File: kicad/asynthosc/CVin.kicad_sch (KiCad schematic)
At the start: 11 parts, among them J14 AudioJack3, SW4 SW_DIP_x02, U9 MCP6004

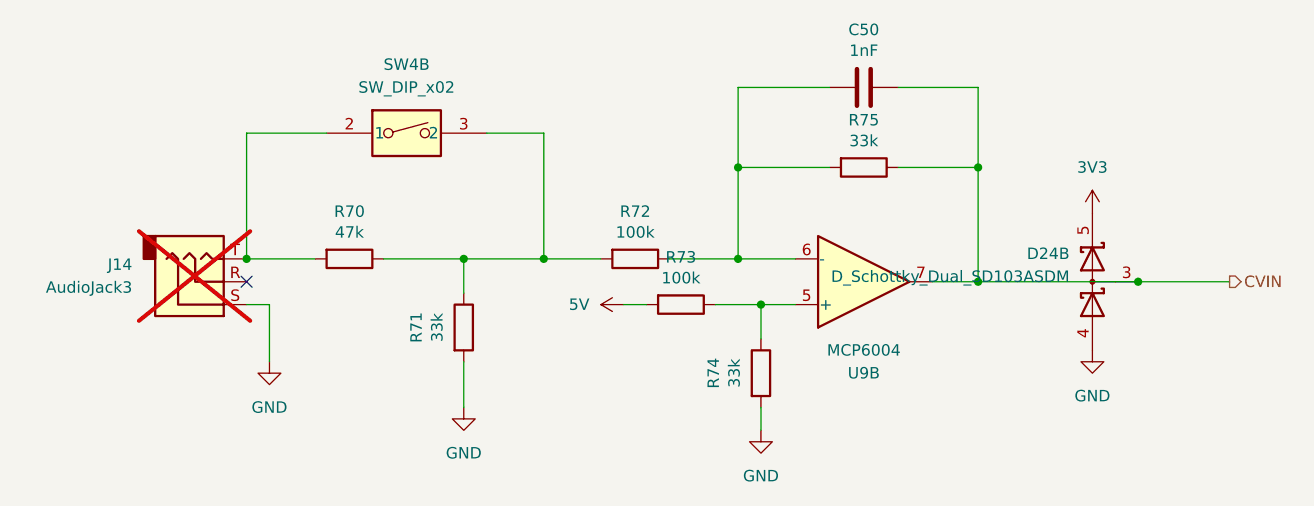
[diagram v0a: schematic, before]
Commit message: bom: fab: switch component due to fab shortage
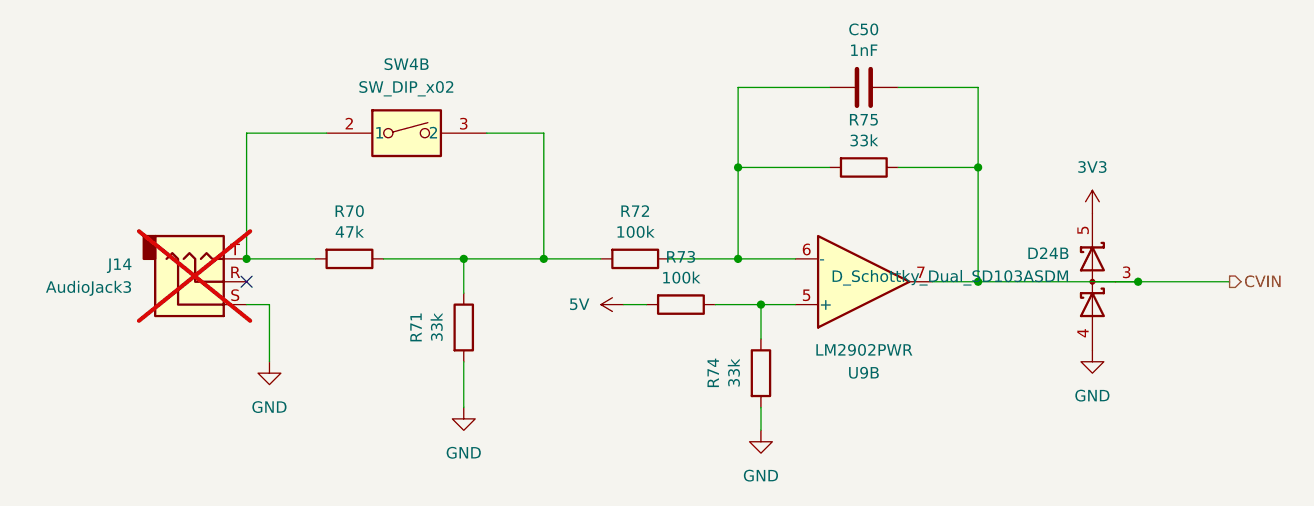
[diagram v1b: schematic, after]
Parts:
- U9: value MCP6004 -> LM2902PWR; LCSC C627416 -> C46864; Manufacturer Microchip -> TI; RefNum MCP6004T-E/ST -> LM2902PWR
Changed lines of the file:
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@@
 			)
 		)
-		(property "Value" "MCP6004"
+		(property "Value" "LM2902PWR"
 			(at 113.03 62.23 0)
 			(effects
@@
 			)
 		)
-		(property "LCSC" "C627416"
+		(property "LCSC" "C46864"
 			(at 113.03 54.61 0)
 			(effects
@@
 			)
 		)
-		(property "Manufacturer" "Microchip"
+		(property "Manufacturer" "TI"
 			(at 113.03 54.61 0)
 			(effects
@@
 			)
 		)
-		(property "RefNum" " MCP6004T-E/ST"
+		(property "RefNum" " LM2902PWR"
 			(at 113.03 54.61 0)
 			(effects

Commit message: sch: bump to kicad 9
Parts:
- renumbered C50 to C34, D24 to D22, J14 to J8, R70 to R27, R71 to R28, R72 to R29, R73 to R30, R74 to R31, R75 to R32, SW4 to SW3, U9 to U8
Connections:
- net 3V3: now also D22.2 (K); no longer D22.5 (K)
- net CVIN: now also D22.6 (common), U8.1; no longer D22.3 (common), U8.7
- net GND: now also D22.1 (A); no longer D22.4 (A)
- net at C34.2, R29.1, R32.2: now also U8.2 (-); no longer U8.6 (-)
- net at R27.1, R28.1, R29.2: now also SW3.4 (2); no longer SW3.3 (2)
- net at J8.T, R27.2: now also SW3.1; no longer SW3.2 (1)
- net at R30.1, R31.1: now also U8.3 (+); no longer U8.5 (+)
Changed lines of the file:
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@@
 (kicad_sch
-	(version 20231120)
+	(version 20250114)
 	(generator "eeschema")
-	(generator_version "8.0")
+	(generator_version "9.0")
 	(paper "A4")
 	(junction
@@
 		(shape output)
 		(at 153.67 54.61 0)
-		(fields_autoplaced yes)
 		(effects
 			(font
@@
 		(dnp no)
 		(fields_autoplaced yes)
-		(property "Reference" "#PWR0124"
+		(property "Reference" "#PWR073"
 			(at 101.6 77.47 0)
 			(effects
@@
 		(dnp no)
 		(fields_autoplaced yes)
-		(property "Reference" "#PWR0123"
+		(property "Reference" "#PWR072"
 			(at 90.17 57.15 0)
 			(effects
@@
 		(on_board yes)
 		(dnp no)
-		(property "Reference" "R75"
+		(property "Reference" "R32"
 			(at 113.03 36.6522 90)
 			(effects
@@
 		(on_board yes)
 		(dnp no)
-		(property "Reference" "R70"
+		(property "Reference" "R27"
 			(at 55.88 46.8122 90)
 			(effects
@@
 		(dnp no)
 		(fields_autoplaced yes)
-		(property "Reference" "#PWR0122"
+		(property "Reference" "#PWR071"
 			(at 68.58 74.93 0)
 			(effects
@@
 		(dnp no)
 		(fields_autoplaced yes)
-		(property "Reference" "#PWR0155"
+		(property "Reference" "#PWR0152"
 			(at 138.43 68.58 0)
 			(effects
@@
 		(lib_id "asynthosc_lib:D_Schottky_Dual_SD103ASDM")
 		(at 138.43 54.61 90)
-		(unit 2)
+		(unit 1)
 		(exclude_from_sim no)
 		(in_bom yes)
@@
 		(dnp no)
 		(fields_autoplaced yes)
-		(property "Reference" "D24"
+		(property "Reference" "D22"
 			(at 135.89 51.4984 90)
 			(effects
@@
 		(lib_id "asynthosc_lib:SW_DIP_x02_SEP")
 		(at 62.23 38.1 0)
-		(unit 2)
+		(unit 1)
 		(exclude_from_sim no)
 		(in_bom yes)
@@
 		(dnp no)
 		(fields_autoplaced yes)
-		(property "Reference" "SW4"
+		(property "Reference" "SW3"
 			(at 62.23 30.48 0)
 			(effects
@@
 		(on_board yes)
 		(dnp yes)
-		(property "Reference" "J14"
+		(property "Reference" "J8"
 			(at 31.75 52.7049 0)
 			(effects
@@
 		(at 113.03 54.61 0)
 		(mirror x)
-		(unit 2)
+		(unit 1)
 		(exclude_from_sim no)
 		(in_bom yes)
 		(on_board yes)
 		(dnp no)
-		(property "Reference" "U9"
+		(property "Reference" "U8"
 			(at 113.03 64.77 0)
 			(effects
@@
 		(on_board yes)
 		(dnp no)
-		(property "Reference" "C50"
+		(property "Reference" "C34"
 			(at 113.03 26.6192 90)
 			(effects
@@
 		(on_board yes)
 		(dnp no)
-		(property "Reference" "R73"
+		(property "Reference" "R30"
 			(at 92.71 51.8922 90)
 			(effects
@@
 		(on_board yes)
 		(dnp no)
-		(property "Reference" "R71"
+		(property "Reference" "R28"
 			(at 63.3222 59.69 90)
 			(effects
@@
 		(on_board yes)
 		(dnp no)
-		(property "Reference" "R74"
+		(property "Reference" "R31"
 			(at 96.3422 64.77 90)
 			(effects
@@
 		(dnp no)
 		(fields_autoplaced yes)
-		(property "Reference" "#PWR0121"
+		(property "Reference" "#PWR070"
 			(at 46.99 69.85 0)
 			(effects
@@
 		(dnp no)
 		(fields_autoplaced yes)
-		(property "Reference" "#PWR0151"
+		(property "Reference" "#PWR0148"
 			(at 138.43 50.8 0)
 			(effects
@@
 		(on_board yes)
 		(dnp no)
-		(property "Reference" "R72"
+		(property "Reference" "R29"
 			(at 87.63 46.8122 90)
 			(effects
